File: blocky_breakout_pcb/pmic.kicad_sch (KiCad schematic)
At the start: 19 parts, among them U5 LM66100DCK, U6 AOZ1280CI, U7 LM66100DCK, U9 TCR2EE11

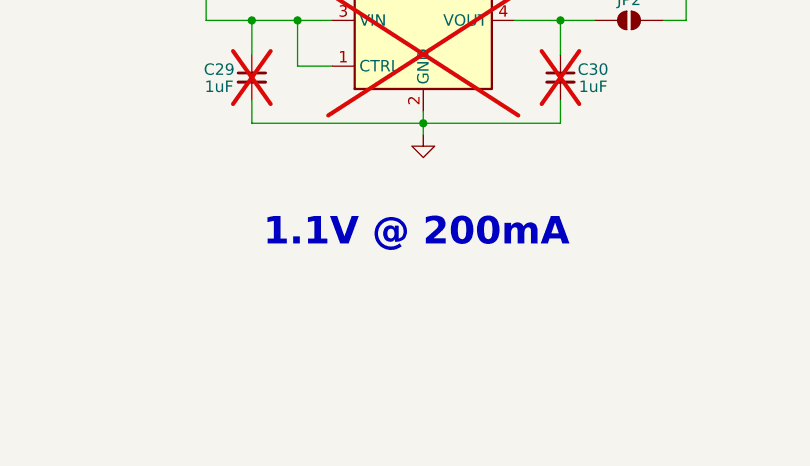
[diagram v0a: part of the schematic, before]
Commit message: Layout nearly finished, entering part numbers
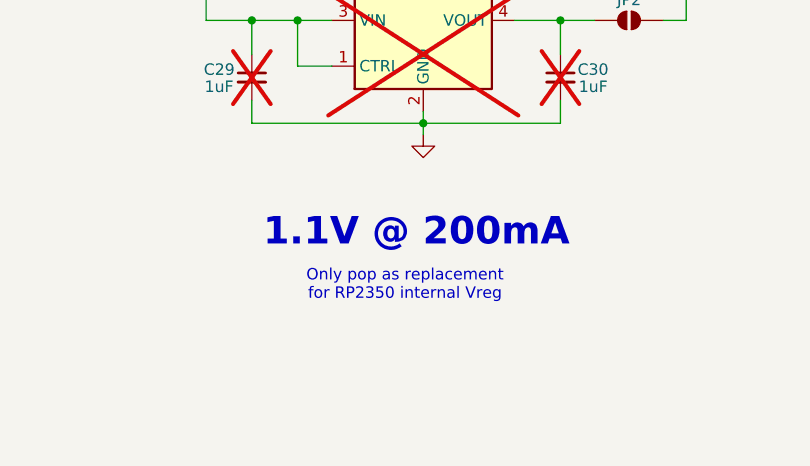
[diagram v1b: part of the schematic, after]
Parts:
- C20, C21, C25, C26: MPN CC0402KRX7R7BB104 -> CL05B104KP5NNNC
- C22: MPN CL10B105KA8NNNC -> JMK105BJ105KV-F
- C29, C30: MPN CC0402KRX7R7BB104 -> JMK105BJ105KV-F
- R11: MPN RT0603BRD07100KL -> RC0402FR-13100KL
- R12: MPN RC0603FR-0749K9L -> RC0402FR-1349K9L
- R13: MPN RC0603FR-079K53L -> RC0402FR-1315K8L
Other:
- note added: "Only pop as replacement for RP2350 internal Vreg"
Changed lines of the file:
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@@
 		)
 	)
+	(text "Only pop as replacement \nfor RP2350 internal Vreg"
+		(exclude_from_sim no)
+		(at 84.328 176.784 0)
+		(effects
+			(font
+				(size 1.27 1.27)
+			)
+		)
+	)
 	(text "3.3V @ 1.2A"
 		(exclude_from_sim no)
@@
 			)
 		)
-		(property "MPN" "CC0402KRX7R7BB104"
+		(property "MPN" "CL05B104KP5NNNC"
 			(at 96.52 40.64 0)
 			(effects
@@
 			)
 		)
-		(property "MPN" "CC0402KRX7R7BB104"
+		(property "MPN" "JMK105BJ105KV-F"
 			(at 102.87 149.86 0)
 			(effects
@@
 			)
 		)
-		(property "MPN" "CC0402KRX7R7BB104"
+		(property "MPN" "CL05B104KP5NNNC"
 			(at 96.52 67.31 0)
 			(effects
@@
 			)
 		)
-		(property "MPN" "CL10B105KA8NNNC"
+		(property "MPN" "JMK105BJ105KV-F"
 			(at 233.045 92.075 0)
 			(effects
@@
 			)
 		)
-		(property "MPN" "CC0402KRX7R7BB104"
+		(property "MPN" "CL05B104KP5NNNC"
 			(at 64.77 39.37 0)
 			(effects
@@
 			)
 		)
-		(property "MPN" "CC0402KRX7R7BB104"
+		(property "MPN" "JMK105BJ105KV-F"
 			(at 66.04 149.86 0)
 			(effects
@@
 			)
 		)
-		(property "MPN" "RC0603FR-079K53L"
+		(property "MPN" "RC0402FR-1315K8L"
 			(at 247.015 104.775 0)
 			(effects
@@
 			)
 		)
-		(property "MPN" "RT0603BRD07100KL"
+		(property "MPN" "RC0402FR-13100KL"
 			(at 204.47 97.155 0)
 			(effects
@@
 			)
 		)
-		(property "MPN" "RC0603FR-0749K9L"
+		(property "MPN" "RC0402FR-1349K9L"
 			(at 247.015 97.79 0)
 			(effects
@@
 			)
 		)
-		(property "MPN" "CC0402KRX7R7BB104"
+		(property "MPN" "CL05B104KP5NNNC"
 			(at 69.85 55.88 0)
 			(effects
